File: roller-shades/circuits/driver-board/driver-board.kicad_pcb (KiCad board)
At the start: 2 copper layers, 40.3 x 50.1 mm, 39 parts, among them J1 1B_Conn, J2 DS18B20, J3 PWR, J4 PROG, J5 WINDOW, J6 1A_Conn, J7 2A_Conn, J8 2B_Conn, U1 AMS1117-3.3, U2 AS5601-ASOM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

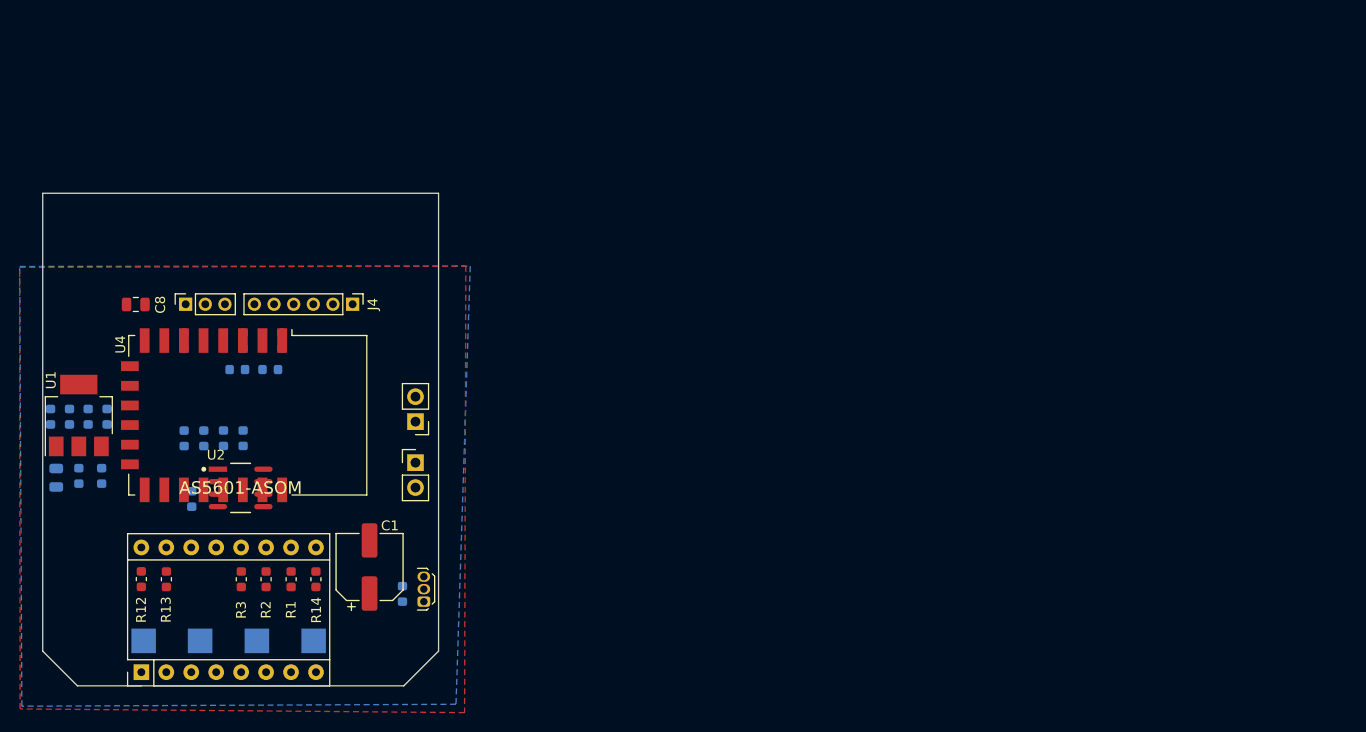
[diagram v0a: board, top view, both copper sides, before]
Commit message: Refractored dependencies into each project and added missing folders
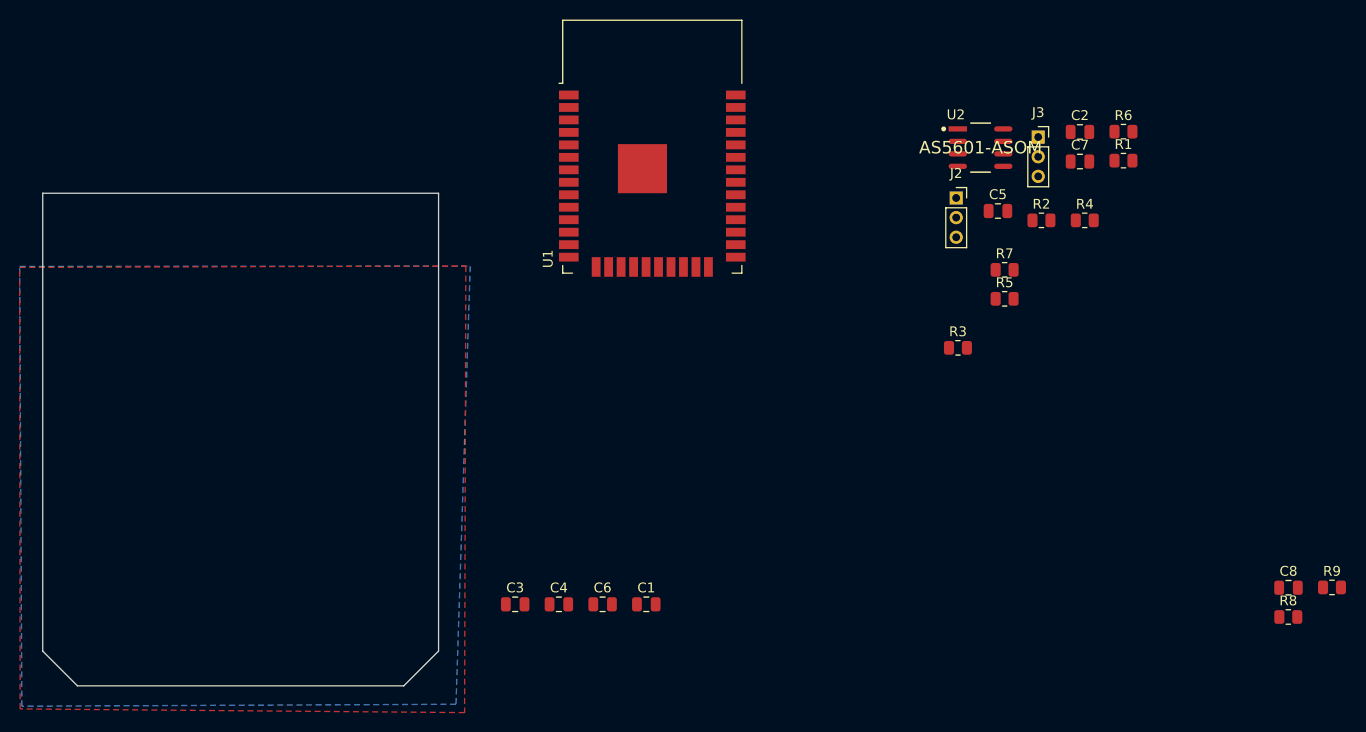
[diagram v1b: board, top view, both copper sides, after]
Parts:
- removed A1: Pololu_Breakout_A4988, Module:Pololu_Breakout-16_15.2x20.3mm
- removed D1: DIODE, Diode_SMD:D_0805_2012Metric
- removed F1: Fuse, Fuse:Fuse_0603_1608Metric
- removed J1: 1B_Conn, TestPoint:TestPoint_Pad_2.5x2.5mm
- removed J4: PROG, Connector_PinHeader_2.00mm:PinHeader_1x06_P2.00mm_Vertical
- removed J5: WINDOW, Connector_PinHeader_2.54mm:PinHeader_1x02_P2.54mm_Vertical
- removed J6: 1A_Conn, TestPoint:TestPoint_Pad_2.5x2.5mm
- removed J7: 2A_Conn, TestPoint:TestPoint_Pad_2.5x2.5mm
- removed J8: 2B_Conn, TestPoint:TestPoint_Pad_2.5x2.5mm
- removed R10, R11, R12, R13, R14, R15, R16: 10k, Resistor_SMD:R_0603_1608Metric
- removed U3: DRV5033A1, Package_TO_SOT_THT:TO-92Flat
- removed U4: ESP-12F, RF_Module:ESP-12E
- C1: value 100µF -> 10µF 50V; footprint Capacitor_SMD:CP_Elec_6.3x7.7 -> Capacitor_SMD:C_0805_2012Metric
- C2, C7: footprint Capacitor_SMD:C_0603_1608Metric -> Capacitor_SMD:C_0805_2012Metric; moved to F.Cu
- C3: value 10µF -> 100nF; footprint Capacitor_SMD:C_0603_1608Metric -> Capacitor_SMD:C_0805_2012Metric; moved to F.Cu
- C4: value 100nF -> 220pF; footprint Capacitor_SMD:C_0603_1608Metric -> Capacitor_SMD:C_0805_2012Metric; moved to F.Cu
- C5: value 100nF -> NS; footprint Capacitor_SMD:C_0603_1608Metric -> Capacitor_SMD:C_0805_2012Metric; moved to F.Cu
- C6: value 10µF -> 22µF 6.3V; footprint Capacitor_SMD:C_0603_1608Metric -> Capacitor_SMD:C_0805_2012Metric; moved to F.Cu
- C8: value 100nF -> 100µF; footprint Fuse:Fuse_0805_2012Metric -> Capacitor_SMD:C_0805_2012Metric
- J2: value DS18B20 -> AUX1
- J3: value PWR -> AUX2; footprint Connector_PinHeader_2.54mm:PinHeader_1x02_P2.54mm_Vertical -> Connector_PinSocket_2.00mm:PinSocket_1x03_P2.00mm_Vertical
- R1: value 10k -> 100K; footprint Resistor_SMD:R_0603_1608Metric -> Resistor_SMD:R_0805_2012Metric
- R2: value 10k -> 24.9K; footprint Resistor_SMD:R_0603_1608Metric -> Resistor_SMD:R_0805_2012Metric
- R3: value 10k -> 200K; footprint Resistor_SMD:R_0603_1608Metric -> Resistor_SMD:R_0805_2012Metric
- R4: value 10k -> 68.1K; footprint Resistor_SMD:R_0603_1608Metric -> Resistor_SMD:R_0805_2012Metric; moved to F.Cu
- R5: value 220k -> 124K; footprint Resistor_SMD:R_0603_1608Metric -> Resistor_SMD:R_0805_2012Metric; moved to F.Cu
- R6: value 100k -> 40.2K; footprint Resistor_SMD:R_0603_1608Metric -> Resistor_SMD:R_0805_2012Metric; moved to F.Cu
- R7: value 1K -> 10K; footprint Resistor_SMD:R_0603_1608Metric -> Resistor_SMD:R_0805_2012Metric; moved to F.Cu
- R8, R9: value 10k -> ??R; footprint Resistor_SMD:R_0603_1608Metric -> Resistor_SMD:R_0805_2012Metric; moved to F.Cu
- U1: value AMS1117-3.3 -> ESP32-WROOM-32; footprint Package_TO_SOT_SMD:SOT-223-3_TabPin2 -> RF_Module:ESP32-WROOM-32
- moved C8 120.8 mm to (167.5, 62.5), turned to 0 degrees
- moved R9 113.7 mm to (171.9, 62.5), turned to 0 degrees
- moved R8 106.2 mm to (167.5, 65.5), turned to 0 degrees
- moved C7 106.1 mm to (146.3, 19.1), turned to 0 degrees
- moved C2 97.8 mm to (146.3, 16.1), turned to 0 degrees
- moved R7 96.6 mm to (138.6, 30.1), turned to 0 degrees
- moved R1 94.9 mm to (150.7, 19.0), turned to 0 degrees
- moved R6 93.4 mm to (150.7, 16.1), turned to 0 degrees
- moved R4 90.5 mm to (146.8, 25.1), turned to 0 degrees
- moved R2 87.0 mm to (142.4, 25.1), turned to 0 degrees
- moved U2 82.9 mm to (136.2, 17.7)
- moved J2 79.2 mm to (133.7, 22.8), turned to 0 degrees
- moved R3 76.7 mm to (133.9, 38.1), turned to 0 degrees
- moved R5 75.1 mm to (138.6, 33.1), turned to 0 degrees
- moved C5 72.1 mm to (137.9, 24.1), turned to 0 degrees
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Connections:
- net /ENC_A renamed /AS5601_ABI_B
- net /ENC_B renamed /AS5601_ABI_A
- C1 pad 1: VDD -> GND
- C1 pad 2: GND -> VBUS
- C3 pad 2: GND -> Net-(C3-Pad2)
- C4 pad 1: Net-(C3-Pad1) -> Net-(C4-Pad1)
- C4 pad 2: GND -> Net-(C4-Pad2)
- C5 pad 1: +3V3 -> Net-(C4-Pad2)
- C8 pad 1: +3V3 -> VBUS
- J2 pad 2: /GPIO12 -> /CONN_AUX1
- J3 pad 2: VDD -> /CONN_AUX2
- R1 pad 1: +3V3 -> Net-(R1-Pad1)
- R1 pad 2: /STPR_MS1 -> VBUS
- R2 pad 1: +3V3 -> GND
- R2 pad 2: /STPR_MS2 -> Net-(R1-Pad1)
- R3 pad 1: +3V3 -> Net-(R3-Pad1)
- R3 pad 2: /STPR_MS3 -> GND
- R4 pad 1: +3V3 -> GND
- R4 pad 2: /I2C_SDA -> Net-(C4-Pad1)
- R5 pad 2: /GPIO_ADC -> +3V3
- R6 pad 1: /GPIO_ADC -> GND
- R6 pad 2: GND -> Net-(R5-Pad1)
- R8 pad 1: +3V3 -> Net-(R8-Pad1)
- R8 pad 2: /RST -> GND
- R9 pad 1: +3V3 -> Net-(R9-Pad1)
- R9 pad 2: Net-(R9-Pad2) -> GND
- U1 pad 1: GND -> Net-(U1-Pad1)
- U1 pad 2: +3V3 -> Net-(U1-Pad2)
- U1 pad 3: Net-(C3-Pad1) -> Net-(U1-Pad3)
